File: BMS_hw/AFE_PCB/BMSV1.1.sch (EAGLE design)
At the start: 286 parts, among them IC1 MC33771BEP, IC10 TLP152-COUPLERTOSHIBA, IC11 TLP152-COUPLERTOSHIBA, IC2 SFH6156-1, IC3 MIC28515V1, IC7 SFH6156-1, IC8 SFH6156-1, IC9 TLP152-COUPLERTOSHIBA, Q1 IRLML5203, Q2 BSS138PW, T1 IPT020N10N3V1, T2 IPT020N10N3V1, T3 IPT020N10N3V1, T4 IPT020N10N3V1, U1 NCP1117LP-PG, U2 NCP1117LP-PG, X5 22-23-2041

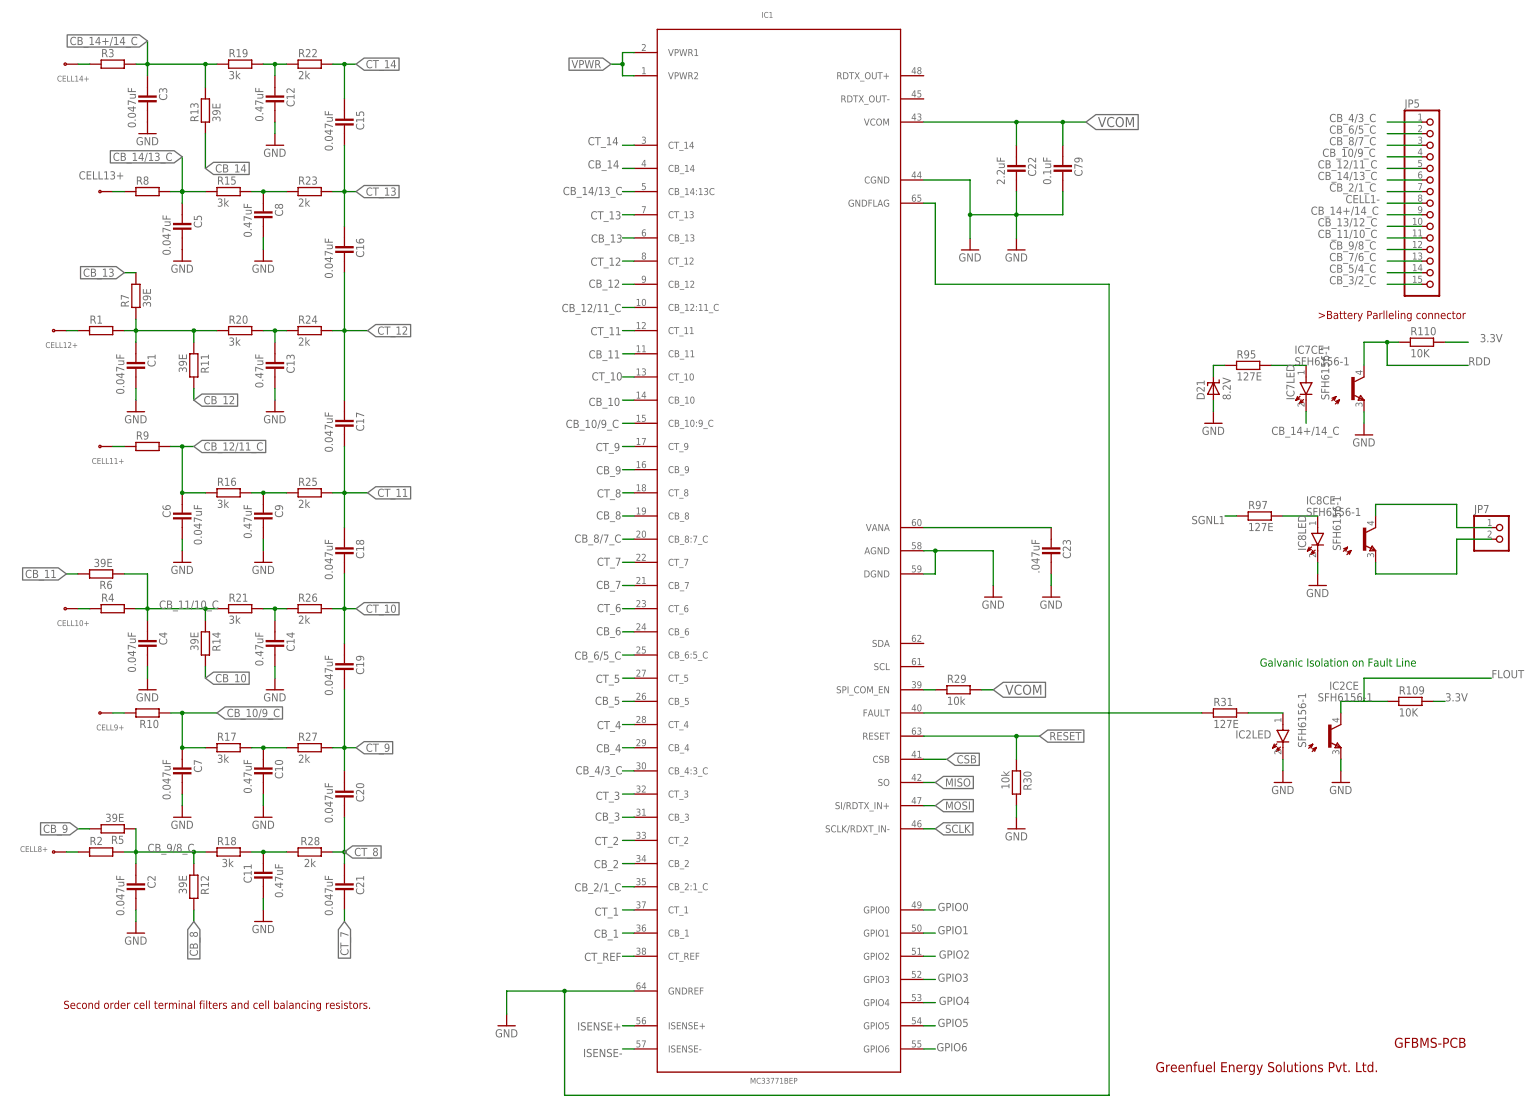
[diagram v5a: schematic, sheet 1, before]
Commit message: AFE master bom itt, layout itt, sch itt
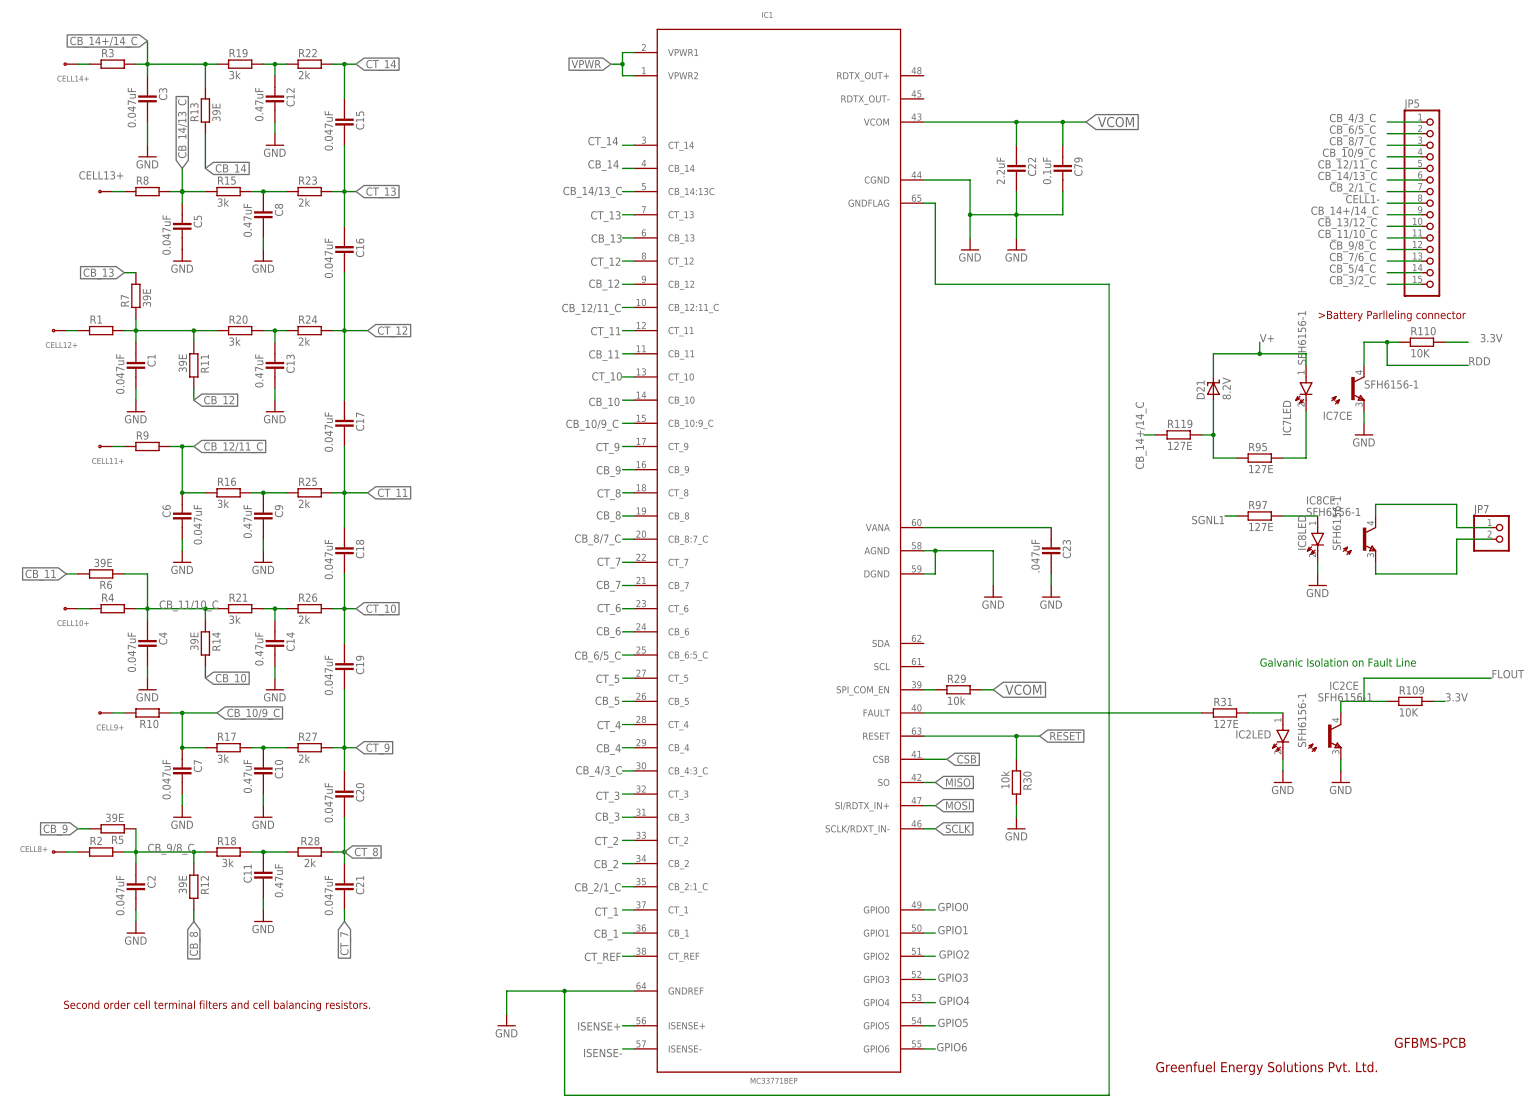
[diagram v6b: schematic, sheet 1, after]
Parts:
- added R119: 127E, ipc-7351-resistor:RESISTOR_0402
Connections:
- removed net +15V: IC10.VCC, IC11.VCC, IC9.VCC
- removed net 15V_AUX: C70.2, C82.2, U1.IN, U2.IN
- removed net VCC: C83.1, C84.1, C85.1, C87.2, C88.1, C91.+, L1.2, R85.1
- new net +12V: C70.2, C82.2, C83.1, C84.1, C85.1, C87.2, C88.1, C91.+, IC10.VCC, IC11.VCC, IC9.VCC, L1.2, R85.1, U1.IN, U2.IN
- net CB_14+/14_C: now also R119.1; no longer IC7LED.K
- net GND: no longer D21.A
- net N$25: now also IC7LED.K; no longer IC7LED.A
- net N$36: now also D21.A, R119.2; no longer D21.K
- net V+: now also D21.K, IC7LED.A
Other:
- moved on the sheet: R95

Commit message: afe board layout and schematic alt!
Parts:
- R1, R10, R2, R3, R32, R33, R36, R37, R38, R4, R41, R42, R43, R8, R9: value (none) -> 0E
- R34: value 0R -> 0E
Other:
- moved on the sheet: CELL1-, R107

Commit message: afe and piggy sch layout itt!
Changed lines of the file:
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@@
 </instance>
 <instance part="C90" gate="G$1" x="236.22" y="139.7" smashed="yes" rot="R90">
-<attribute name="NAME" x="234.188" y="137.16" size="1.778" layer="95" rot="R90"/>
+<attribute name="NAME" x="234.188" y="137.16" size="1.778" layer="95" font="vector" ratio="12" rot="R90"/>
 <attribute name="VALUE" x="232.41" y="137.16" size="1.778" layer="96" rot="R90"/>
 </instance>
